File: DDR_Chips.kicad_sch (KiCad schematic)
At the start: 1 part

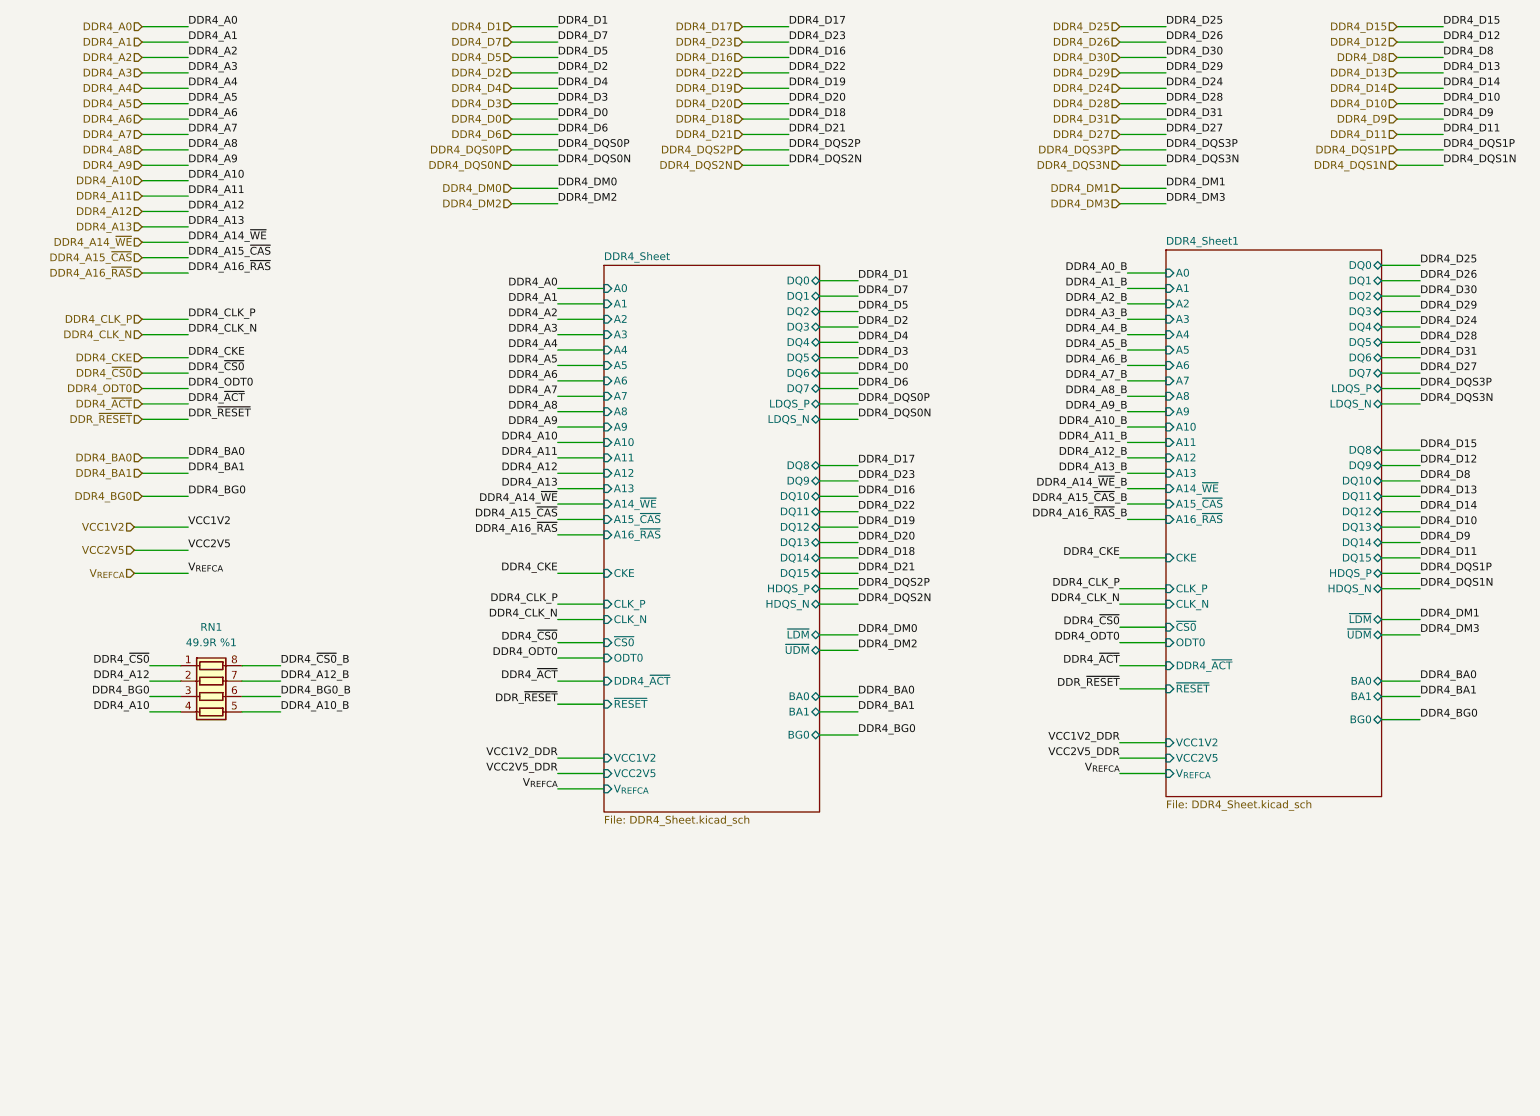
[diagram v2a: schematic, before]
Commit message: remove DRC errors
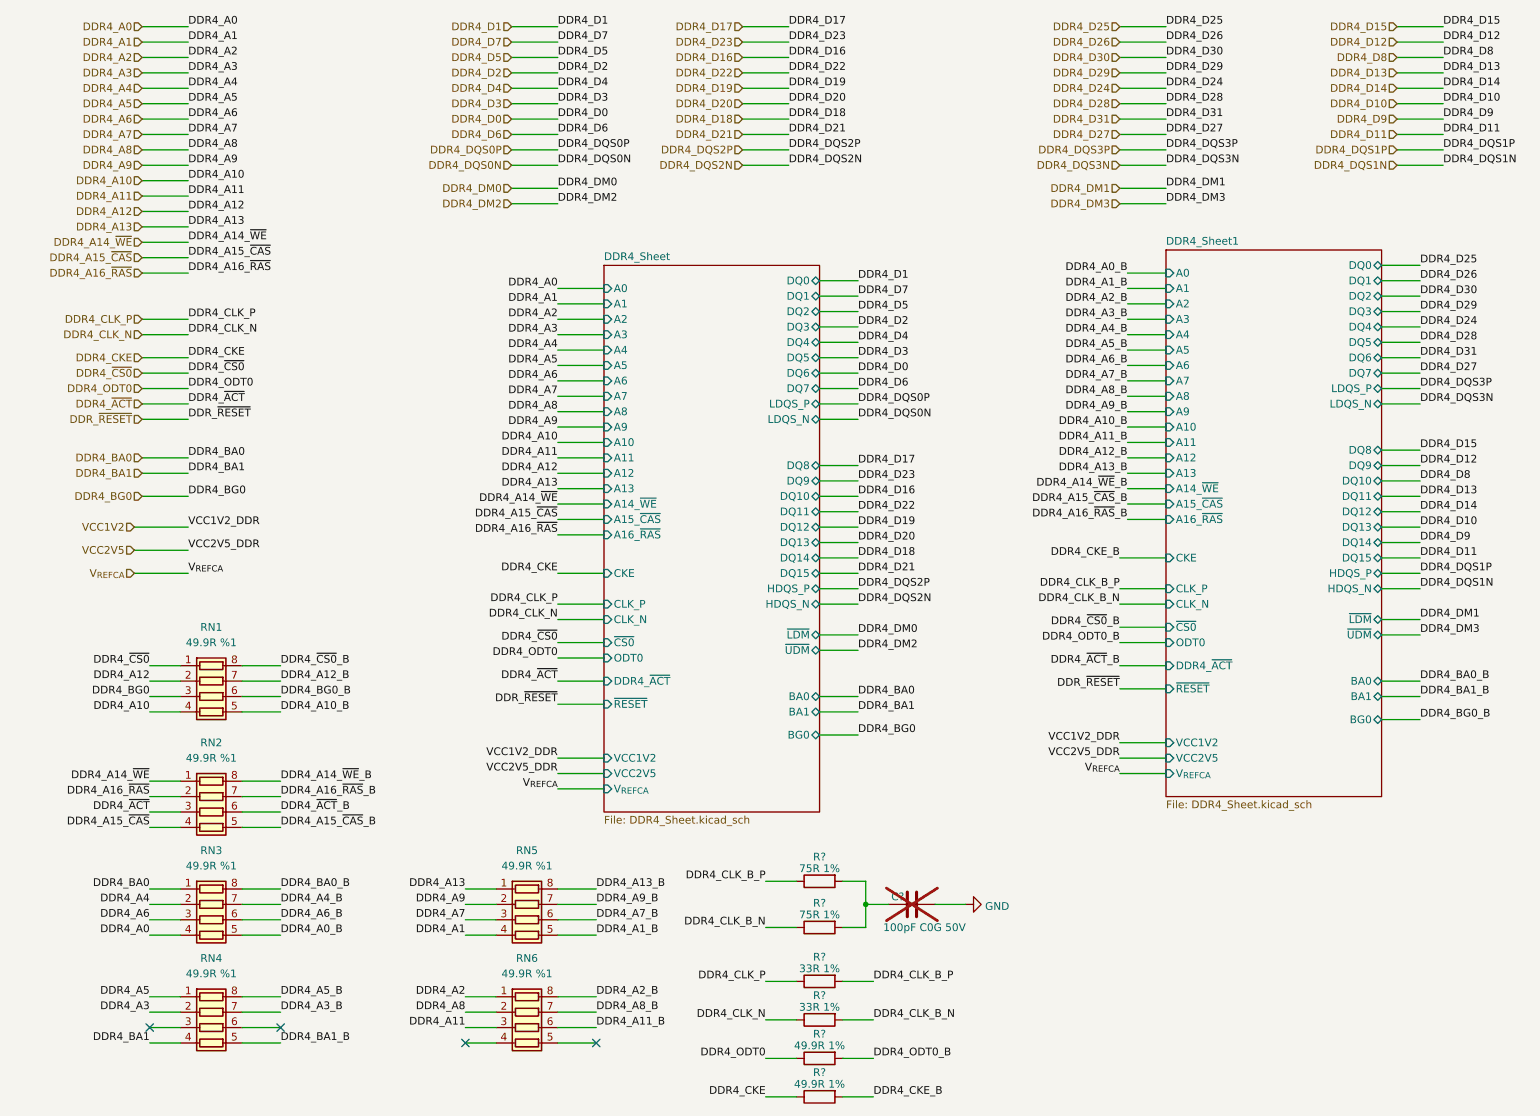
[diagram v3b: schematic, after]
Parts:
- added C?: 100pF C0G 50V, Capacitor_SMD:C_0201_0603Metric, symbol Device:C
- added R? (x2): 49.9R 1%, Resistor_SMD:R_0402_1005Metric, symbol Device:R
- added R? (x2): 75R 1%, Resistor_SMD:R_0402_1005Metric, symbol Device:R
- added R? (x2): 33R 1%, Resistor_SMD:R_0402_1005Metric, symbol Device:R
- added RN2, RN3, RN4, RN5, RN6: 49.9R %1, symbol Device:R_Pack04
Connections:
- net DDR4_A0: now also RN3.4 (R4.1)
- net DDR4_A0_B: now also RN3.5 (R4.2)
- net DDR4_A1: now also RN5.4 (R4.1)
- net DDR4_A11: now also RN6.3 (R3.1)
- net DDR4_A11_B: now also RN6.6 (R3.2)
- net DDR4_A13: now also RN5.1 (R1.1)
- net DDR4_A13_B: now also RN5.8 (R1.2)
- net DDR4_A14_~{WE}: now also RN2.1 (R1.1)
- net DDR4_A14_~{WE}_B: now also RN2.8 (R1.2)
- net DDR4_A15_~{CAS}: now also RN2.4 (R4.1)
- net DDR4_A15_~{CAS}_B: now also RN2.5 (R4.2)
- net DDR4_A16_~{RAS}: now also RN2.2 (R2.1)
- net DDR4_A16_~{RAS}_B: now also RN2.7 (R2.2)
- net DDR4_A1_B: now also RN5.5 (R4.2)
- net DDR4_A2: now also RN6.1 (R1.1)
- net DDR4_A2_B: now also RN6.8 (R1.2)
- net DDR4_A3: now also RN4.2 (R2.1)
- net DDR4_A3_B: now also RN4.7 (R2.2)
- net DDR4_A4: now also RN3.2 (R2.1)
- net DDR4_A4_B: now also RN3.7 (R2.2)
- net DDR4_A5: now also RN4.1 (R1.1)
- net DDR4_A5_B: now also RN4.8 (R1.2)
- net DDR4_A6: now also RN3.3 (R3.1)
- net DDR4_A6_B: now also RN3.6 (R3.2)
- net DDR4_A7: now also RN5.3 (R3.1)
- net DDR4_A7_B: now also RN5.6 (R3.2)
- net DDR4_A8: now also RN6.2 (R2.1)
- net DDR4_A8_B: now also RN6.7 (R2.2)
- net DDR4_A9: now also RN5.2 (R2.1)
- net DDR4_A9_B: now also RN5.7 (R2.2)
- net DDR4_BA0: now also RN3.1 (R1.1)
- net DDR4_BA1: now also RN4.4 (R4.1)
- net DDR4_CKE: now also R?.1
- net DDR4_CLK_N: now also R?.1
- net DDR4_CLK_P: now also R?.1
- net DDR4_ODT0: now also R?.1
- net DDR4_~{ACT}: now also RN2.3 (R3.1)
- new net: C?.1, R?.2, R?.2
- new net DDR4_BA0_B: RN3.8 (R1.2)
- new net DDR4_BA1_B: RN4.5 (R4.2)
- new net DDR4_CKE_B: R?.2
- new net DDR4_CLK_B_N: R?.1, R?.2
- new net DDR4_CLK_B_P: R?.1, R?.2
- new net DDR4_ODT0_B: R?.2
- new net DDR4_~{ACT}_B: RN2.6 (R3.2)
- new net GND: C?.2
- no-connect marks 0 -> 4

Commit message: remove all warnings
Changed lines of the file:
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@@
     (effects (font (size 1.27 1.27)) (justify right))
   )
-  (hierarchical_label "VCC2V5" (shape input) (at 29.21 105.41 180) (fields_autoplaced)
+  (hierarchical_label "VCC2V5_DDR" (shape input) (at 29.21 105.41 180) (fields_autoplaced)
     (effects (font (size 1.27 1.27)) (justify right))
   )
@@
     (effects (font (size 1.27 1.27)) (justify right))
   )
-  (hierarchical_label "VCC1V2" (shape input) (at 29.21 101.6 180) (fields_autoplaced)
+  (hierarchical_label "VCC1V2_DDR" (shape input) (at 29.21 101.6 180) (fields_autoplaced)
     (effects (font (size 1.27 1.27)) (justify right))
   )

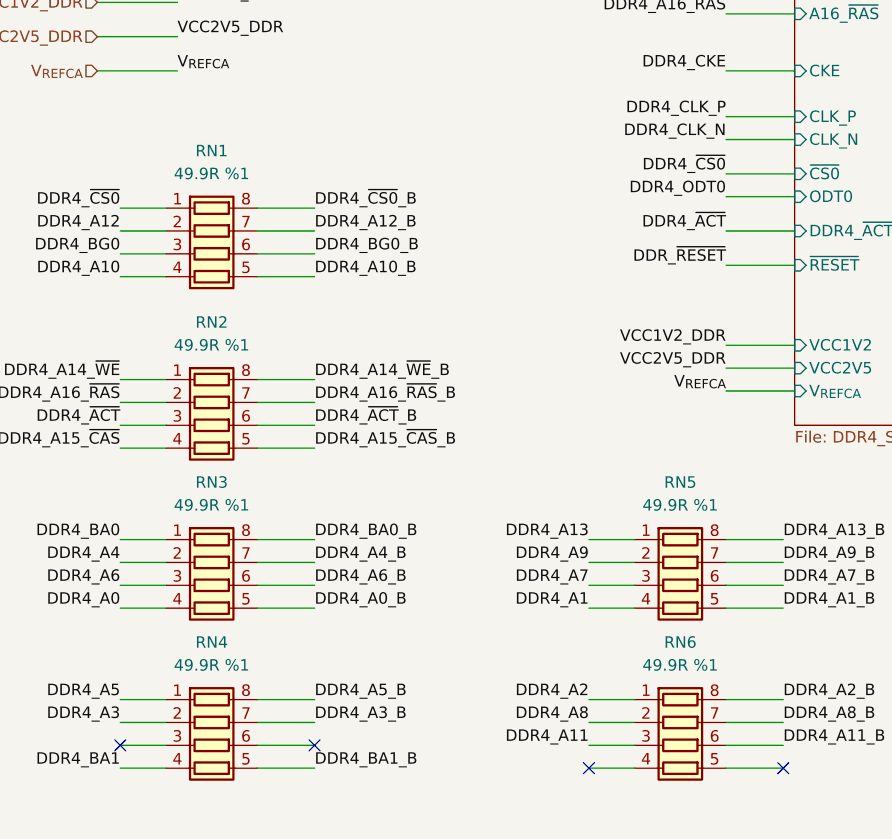
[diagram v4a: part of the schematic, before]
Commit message: update components footprint and LCSC; update RV1126 symbol
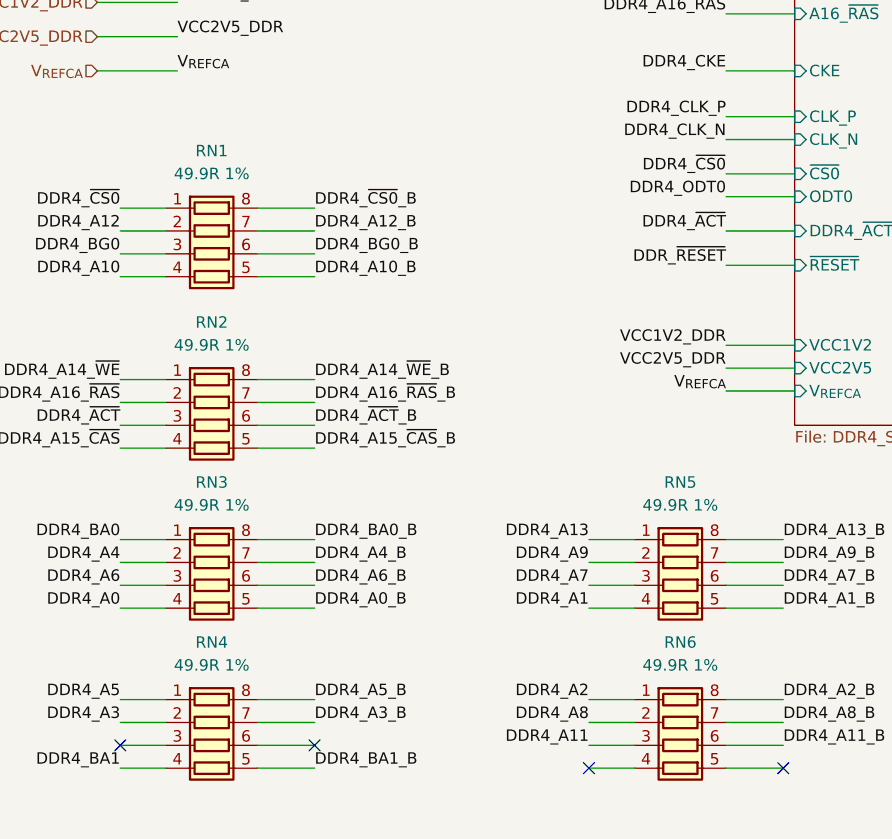
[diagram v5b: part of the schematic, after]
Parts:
- RN1, RN2, RN3, RN4, RN5, RN6: value 49.9R %1 -> 49.9R 1%; footprint (none) -> Resistor_SMD:R_Array_Concave_4x0402; LCSC (none) -> C136850; Model (none) -> YC124-FR-0749R9L; Vendor (none) -> YAGEO(国巨)
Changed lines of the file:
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@@
       (effects (font (size 1.27 1.27)))
     )
-    (property "Value" "49.9R %1" (at 41.91 139.7 90)
-      (effects (font (size 1.27 1.27)))
-    )
-    (property "Footprint" "" (at 41.91 155.575 90)
+    (property "Value" "49.9R 1%" (at 41.91 139.7 90)
+      (effects (font (size 1.27 1.27)))
+    )
+    (property "Footprint" "Resistor_SMD:R_Array_Concave_4x0402" (at 41.91 155.575 90)
       (effects (font (size 1.27 1.27)) hide)
     )
@@
       (effects (font (size 1.27 1.27)) hide)
     )
-    (property "LCSC" "" (at 41.91 148.59 0)
-      (effects (font (size 1.27 1.27)) hide)
-    )
-    (property "Description" "" (at 41.91 148.59 0)
-      (effects (font (size 1.27 1.27)) hide)
-    )
-    (property "Vendor" "" (at 41.91 148.59 0)
+    (property "LCSC" "C136850" (at 41.91 148.59 0)
+      (effects (font (size 1.27 1.27)) hide)
+    )
+    (property "Description" "阻值: 49.9Ω 精度: ±1% 单个元件功率: 62.5mW 电阻器数: 4 引脚数: 8 温度系数: ±200ppm/℃" (at 41.91 148.59 0)
+      (effects (font (size 1.27 1.27)) hide)
+    )
+    (property "Vendor" "YAGEO(国巨)" (at 41.91 148.59 0)
+      (effects (font (size 1.27 1.27)) hide)
+    )
+    (property "Model" "YC124-FR-0749R9L" (at 41.91 148.59 0)
       (effects (font (size 1.27 1.27)) hide)
     )
@@
       (effects (font (size 1.27 1.27)))
     )
-    (property "Value" "49.9R %1" (at 41.91 120.65 90)
-      (effects (font (size 1.27 1.27)))
-    )
-    (property "Footprint" "" (at 41.91 136.525 90)
+    (property "Value" "49.9R 1%" (at 41.91 120.65 90)
+      (effects (font (size 1.27 1.27)))
+    )
+    (property "Footprint" "Resistor_SMD:R_Array_Concave_4x0402" (at 41.91 136.525 90)
       (effects (font (size 1.27 1.27)) hide)
     )
@@
       (effects (font (size 1.27 1.27)) hide)
     )
-    (property "LCSC" "" (at 41.91 129.54 0)
-      (effects (font (size 1.27 1.27)) hide)
-    )
-    (property "Description" "" (at 41.91 129.54 0)
-      (effects (font (size 1.27 1.27)) hide)
-    )
-    (property "Vendor" "" (at 41.91 129.54 0)
+    (property "LCSC" "C136850" (at 41.91 129.54 0)
+      (effects (font (size 1.27 1.27)) hide)
+    )
+    (property "Description" "阻值: 49.9Ω 精度: ±1% 单个元件功率: 62.5mW 电阻器数: 4 引脚数: 8 温度系数: ±200ppm/℃" (at 41.91 129.54 0)
+      (effects (font (size 1.27 1.27)) hide)
+    )
+    (property "Vendor" "YAGEO(国巨)" (at 41.91 129.54 0)
+      (effects (font (size 1.27 1.27)) hide)
+    )
+    (property "Model" "YC124-FR-0749R9L" (at 41.91 129.54 0)
       (effects (font (size 1.27 1.27)) hide)
     )
@@
       (effects (font (size 1.27 1.27)))
     )
-    (property "Value" "49.9R %1" (at 41.91 157.48 90)
-      (effects (font (size 1.27 1.27)))
-    )
-    (property "Footprint" "" (at 41.91 173.355 90)
+    (property "Value" "49.9R 1%" (at 41.91 157.48 90)
+      (effects (font (size 1.27 1.27)))
+    )
+    (property "Footprint" "Resistor_SMD:R_Array_Concave_4x0402" (at 41.91 173.355 90)
       (effects (font (size 1.27 1.27)) hide)
     )
@@
       (effects (font (size 1.27 1.27)) hide)
     )
-    (property "LCSC" "" (at 41.91 166.37 0)
-      (effects (font (size 1.27 1.27)) hide)
-    )
-    (property "Description" "" (at 41.91 166.37 0)
-      (effects (font (size 1.27 1.27)) hide)
-    )
-    (property "Vendor" "" (at 41.91 166.37 0)
+    (property "LCSC" "C136850" (at 41.91 166.37 0)
+      (effects (font (size 1.27 1.27)) hide)
+    )
+    (property "Description" "阻值: 49.9Ω 精度: ±1% 单个元件功率: 62.5mW 电阻器数: 4 引脚数: 8 温度系数: ±200ppm/℃" (at 41.91 166.37 0)
+      (effects (font (size 1.27 1.27)) hide)
+    )
+    (property "Vendor" "YAGEO(国巨)" (at 41.91 166.37 0)
+      (effects (font (size 1.27 1.27)) hide)
+    )
+    (property "Model" "YC124-FR-0749R9L" (at 41.91 166.37 0)
       (effects (font (size 1.27 1.27)) hide)
     )
@@
       (effects (font (size 1.27 1.27)))
     )
-    (property "Value" "49.9R %1" (at 93.98 175.26 90)
-      (effects (font (size 1.27 1.27)))
-    )
-    (property "Footprint" "" (at 93.98 191.135 90)
+    (property "Value" "49.9R 1%" (at 93.98 175.26 90)
+      (effects (font (size 1.27 1.27)))
+    )
+    (property "Footprint" "Resistor_SMD:R_Array_Concave_4x0402" (at 93.98 191.135 90)
       (effects (font (size 1.27 1.27)) hide)
     )
@@
       (effects (font (size 1.27 1.27)) hide)
     )
-    (property "LCSC" "" (at 93.98 184.15 0)
-      (effects (font (size 1.27 1.27)) hide)
-    )
-    (property "Description" "" (at 93.98 184.15 0)
-      (effects (font (size 1.27 1.27)) hide)
-    )
-    (property "Vendor" "" (at 93.98 184.15 0)
+    (property "LCSC" "C136850" (at 93.98 184.15 0)
+      (effects (font (size 1.27 1.27)) hide)
+    )
+    (property "Description" "阻值: 49.9Ω 精度: ±1% 单个元件功率: 62.5mW 电阻器数: 4 引脚数: 8 温度系数: ±200ppm/℃" (at 93.98 184.15 0)
+      (effects (font (size 1.27 1.27)) hide)
+    )
+    (property "Vendor" "YAGEO(国巨)" (at 93.98 184.15 0)
+      (effects (font (size 1.27 1.27)) hide)
+    )
+    (property "Model" "YC124-FR-0749R9L" (at 93.98 184.15 0)
       (effects (font (size 1.27 1.27)) hide)
     )
@@
       (effects (font (size 1.27 1.27)))
     )
-    (property "Value" "49.9R %1" (at 93.98 157.48 90)
-      (effects (font (size 1.27 1.27)))
-    )
-    (property "Footprint" "" (at 93.98 173.355 90)
+    (property "Value" "49.9R 1%" (at 93.98 157.48 90)
+      (effects (font (size 1.27 1.27)))
+    )
+    (property "Footprint" "Resistor_SMD:R_Array_Concave_4x0402" (at 93.98 173.355 90)
       (effects (font (size 1.27 1.27)) hide)
     )
@@
       (effects (font (size 1.27 1.27)) hide)
     )
-    (property "LCSC" "" (at 93.98 166.37 0)
-      (effects (font (size 1.27 1.27)) hide)
-    )
-    (property "Description" "" (at 93.98 166.37 0)
-      (effects (font (size 1.27 1.27)) hide)
-    )
-    (property "Vendor" "" (at 93.98 166.37 0)
+    (property "LCSC" "C136850" (at 93.98 166.37 0)
+      (effects (font (size 1.27 1.27)) hide)
+    )
+    (property "Description" "阻值: 49.9Ω 精度: ±1% 单个元件功率: 62.5mW 电阻器数: 4 引脚数: 8 温度系数: ±200ppm/℃" (at 93.98 166.37 0)
+      (effects (font (size 1.27 1.27)) hide)
+    )
+    (property "Vendor" "YAGEO(国巨)" (at 93.98 166.37 0)
+      (effects (font (size 1.27 1.27)) hide)
+    )
+    (property "Model" "YC124-FR-0749R9L" (at 93.98 166.37 0)
       (effects (font (size 1.27 1.27)) hide)
     )
@@
       (effects (font (size 1.27 1.27)))
     )
-    (property "Value" "49.9R %1" (at 41.91 175.26 90)
-      (effects (font (size 1.27 1.27)))
-    )
-    (property "Footprint" "" (at 41.91 191.135 90)
+    (property "Value" "49.9R 1%" (at 41.91 175.26 90)
+      (effects (font (size 1.27 1.27)))
+    )
+    (property "Footprint" "Resistor_SMD:R_Array_Concave_4x0402" (at 41.91 191.135 90)
       (effects (font (size 1.27 1.27)) hide)
     )
@@
       (effects (font (size 1.27 1.27)) hide)
     )
-    (property "LCSC" "" (at 41.91 184.15 0)
-      (effects (font (size 1.27 1.27)) hide)
-    )
-    (property "Description" "" (at 41.91 184.15 0)
-      (effects (font (size 1.27 1.27)) hide)
-    )
-    (property "Vendor" "" (at 41.91 184.15 0)
-      (effects (font (size 1.27 1.27)) hide)
-    )
+    (property "LCSC" "C136850" (at 41.91 184.15 0)
+      (effects (font (size 1.27 1.27)) hide)
+    )
+    (property "Description" "阻值: 49.9Ω 精度: ±1% 单个元件功率: 62.5mW 电阻器数: 4 引脚数: 8 温度系数: ±200ppm/℃" (at 41.91 184.15 0)
+      (effects (font (size 1.27 1.27)) hide)
+    )
+    (property "Vendor" "YAGEO(国巨)" (at 41.91 184.15 0)
+      (effects (font (size 1.27 1.27)) hide)
+    )
+    (property "Model" "YC124-FR-0749R9L" (at 41.91 184.15 0)
+      (effects (font (size 1.27 1.27)) hide)
+    )
